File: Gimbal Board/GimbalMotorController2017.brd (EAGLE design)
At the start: 86.5 x 101.6 mm, 123 parts, among them J1 SL03THROUGH_HOLE, J3 APP_2POS_CONFIG5V_HORIZ, Q1 Q_IRF7437SMD, Q2 Q_IRF7437SMD, Q3 Q_IRF7437SMD, Q4 Q_IRF7437SMD, Q5 Q_IRF7437SMD, Q6 Q_IRF7437SMD, Q7 MOSFET-PCHANNEL, Q8 MOSFET-PCHANNEL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

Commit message: Fixed ERC issue
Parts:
- R14, R19, R24, R26: value 184k -> 191k
- R15, R20, R25, R27: value 50k -> 51.7k
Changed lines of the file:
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@@
 <attribute name="VALUE" x="71.34225" y="60.67425" size="0.4064" layer="27" font="vector" rot="R270"/>
 </element>
-<element name="R14" library="SparkFun-Passives" package="0805" value="184k" x="56.8325" y="39.0525" smashed="yes" rot="R180">
+<element name="R14" library="SparkFun-Passives" package="0805" value="191k" x="56.8325" y="39.0525" smashed="yes" rot="R180">
 <attribute name="NAME" x="54.737" y="39.8145" size="0.6096" layer="25" font="vector" rot="R270"/>
 <attribute name="VALUE" x="57.0865" y="40.1955" size="0.4064" layer="27" font="vector" rot="R180"/>
 </element>
-<element name="R15" library="SparkFun-Passives" package="0805" value="50k" x="56.8325" y="41.5925" smashed="yes">
+<element name="R15" library="SparkFun-Passives" package="0805" value="51.7k" x="56.8325" y="41.5925" smashed="yes">
 <attribute name="NAME" x="55.626" y="41.3385" size="0.6096" layer="25" font="vector" rot="R90"/>
 <attribute name="VALUE" x="55.8165" y="42.2275" size="0.4064" layer="27" font="vector"/>
@@
 <attribute name="VALUE" x="72.644" y="37.56025" size="0.4064" layer="27" font="vector" rot="R270"/>
 </element>
-<element name="R19" library="SparkFun-Passives" package="0805" value="184k" x="52.2605" y="39.0525" smashed="yes">
+<element name="R19" library="SparkFun-Passives" package="0805" value="191k" x="52.2605" y="39.0525" smashed="yes">
 <attribute name="NAME" x="50.8" y="38.5445" size="0.6096" layer="25" font="vector" rot="R90"/>
 <attribute name="VALUE" x="50.9905" y="39.9415" size="0.4064" layer="27" font="vector"/>
@@
 <attribute name="VALUE" x="38.1" y="42.2275" size="0.4064" layer="27" font="vector" rot="R270"/>
 </element>
-<element name="R20" library="SparkFun-Passives" package="0805" value="50k" x="52.2605" y="41.5925" smashed="yes" rot="R180">
+<element name="R20" library="SparkFun-Passives" package="0805" value="51.7k" x="52.2605" y="41.5925" smashed="yes" rot="R180">
 <attribute name="NAME" x="50.165" y="42.3545" size="0.6096" layer="25" font="vector" rot="R270"/>
 <attribute name="VALUE" x="52.5145" y="42.7355" size="0.4064" layer="27" font="vector" rot="R180"/>
@@
 <attribute name="VALUE" x="34.13125" y="68.961" size="0.4064" layer="27" font="vector" rot="R90"/>
 </element>
-<element name="R24" library="SparkFun-Passives" package="0805" value="184k" x="47.4345" y="39.0525" smashed="yes">
+<element name="R24" library="SparkFun-Passives" package="0805" value="191k" x="47.4345" y="39.0525" smashed="yes">
 <attribute name="NAME" x="45.974" y="38.5445" size="0.6096" layer="25" font="vector" rot="R90"/>
 <attribute name="VALUE" x="46.1645" y="39.9415" size="0.4064" layer="27" font="vector"/>
 </element>
-<element name="R25" library="SparkFun-Passives" package="0805" value="50k" x="47.4345" y="41.5925" smashed="yes" rot="R180">
+<element name="R25" library="SparkFun-Passives" package="0805" value="51.7k" x="47.4345" y="41.5925" smashed="yes" rot="R180">
 <attribute name="NAME" x="45.339" y="42.6085" size="0.6096" layer="25" font="vector" rot="R270"/>
 <attribute name="VALUE" x="47.6885" y="42.7355" size="0.4064" layer="27" font="vector" rot="R180"/>
 </element>
-<element name="R26" library="SparkFun-Passives" package="0805" value="184k" x="61.6585" y="39.0525" smashed="yes" rot="R180">
+<element name="R26" library="SparkFun-Passives" package="0805" value="191k" x="61.6585" y="39.0525" smashed="yes" rot="R180">
 <attribute name="NAME" x="59.563" y="39.8145" size="0.6096" layer="25" font="vector" rot="R270"/>
 <attribute name="VALUE" x="62.1665" y="40.1955" size="0.4064" layer="27" font="vector" rot="R180"/>
 </element>
-<element name="R27" library="SparkFun-Passives" package="0805" value="50k" x="61.6585" y="41.5925" smashed="yes">
+<element name="R27" library="SparkFun-Passives" package="0805" value="51.7k" x="61.6585" y="41.5925" smashed="yes">
 <attribute name="NAME" x="59.69" y="41.7195" size="0.6096" layer="25" font="vector" rot="R270"/>
 <attribute name="VALUE" x="60.6425" y="42.4815" size="0.4064" layer="27" font="vector"/>

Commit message: Updated resistor values for new divider, updated indicators section, changed PWM_IN_NO_FILTER to PWM_IN and removed previous PWM_IN label
Resistor values updated for 12v to 3.2v ratio. Simplified D6 indicator schematic to be just an LED, resistor, power, and ground. Changed old PWM_IN_NO_FILTER label to PWM_IN in external connections, and removed old PWM_IN label from PA2 pin in external connections.
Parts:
- removed D16: 15V, SparkFun-DiscreteSemi:SOD-323
- removed Q9: MOSFET-NCHANNELAO3404A, SparkFun-DiscreteSemi:SOT23-3
- removed R50: 3M, SparkFun-Passives:0805
- removed R51: 1M, SparkFun-Passives:0805
- Q1, Q2, Q3, Q4, Q5, Q6: value Q_IRF7437SMD -> R6020ENJSMD
- R14, R19, R24, R26: value 191k -> 187k
- R15, R20, R25, R27: value 51.7k -> 68.1k
- R32: value 330 -> 1.2k
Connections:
- removed net N$36: C15.1
- removed net N$38: D16.C, Q9.1, R50.2, R51.1
- removed net N$41: D16.A, D6.A, Q9.2
- removed net PWM_IN_NO_FILTER: J1.3, U$2.PF4
- net GND: no longer R51.2
- net PVDD: now also C15.1, D6.A; no longer R50.1
- net PWM_IN: now also J1.3, U$2.PF4; no longer U$2.PA2
- net VCC: no longer Q9.3
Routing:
- net PWM_IN_NO_FILTER: track 17.7 -> 0.00 mm
- net PWM_IN: track 0.00 -> 17.7 mm
- net N$41: track 10.5 -> 0.00 mm
- net VCC: track 212.8 -> 202.4 mm
- net N$38: track 5.40 -> 0.00 mm
- net PVDD: track 79.1 -> 82.2 mm, vias 8 -> 7

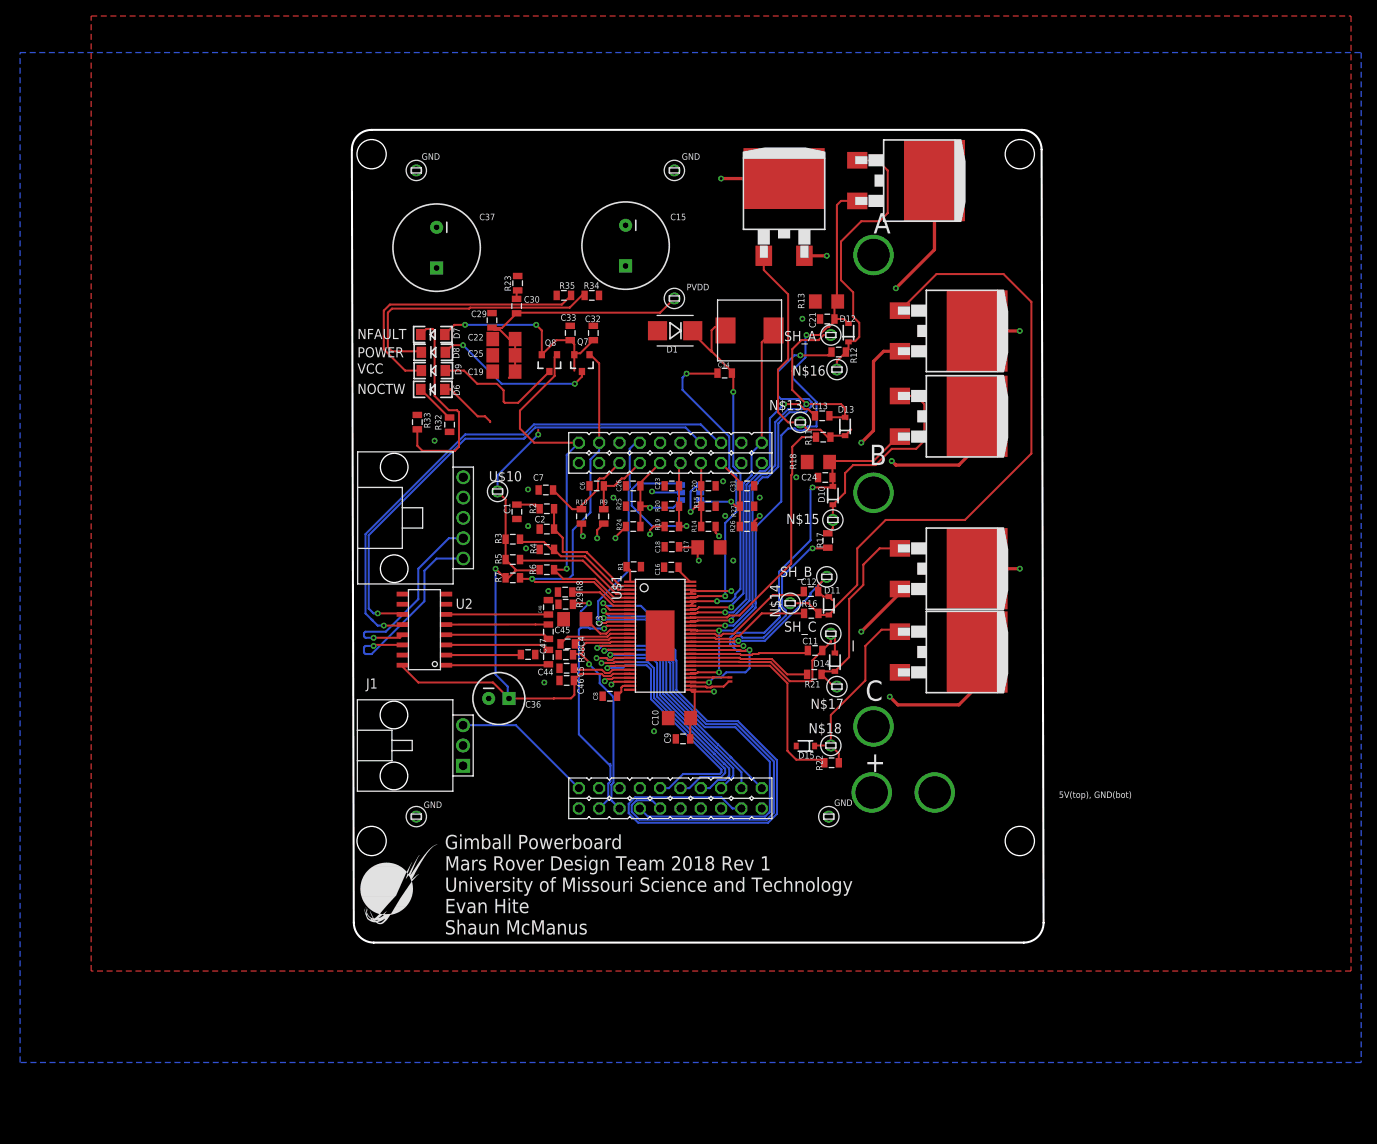
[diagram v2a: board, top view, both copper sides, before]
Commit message: Board routing was cleaned up. Silkscreen was cleaned up. Correct Package for Power Anderson Connectors is now being used.
Mounting holes were removed.  SL connectors were labelled. All test points are correctly named. More vias have been added to stitch the planes together. Traces were redrawn in many places for cleaner paths. Correct Vertical mounting board has been added. Anderson Power Package was changed to correct package. The inductor was moved to reduce noise. The power conditioning capacitor was moved out from under where the control card sits.
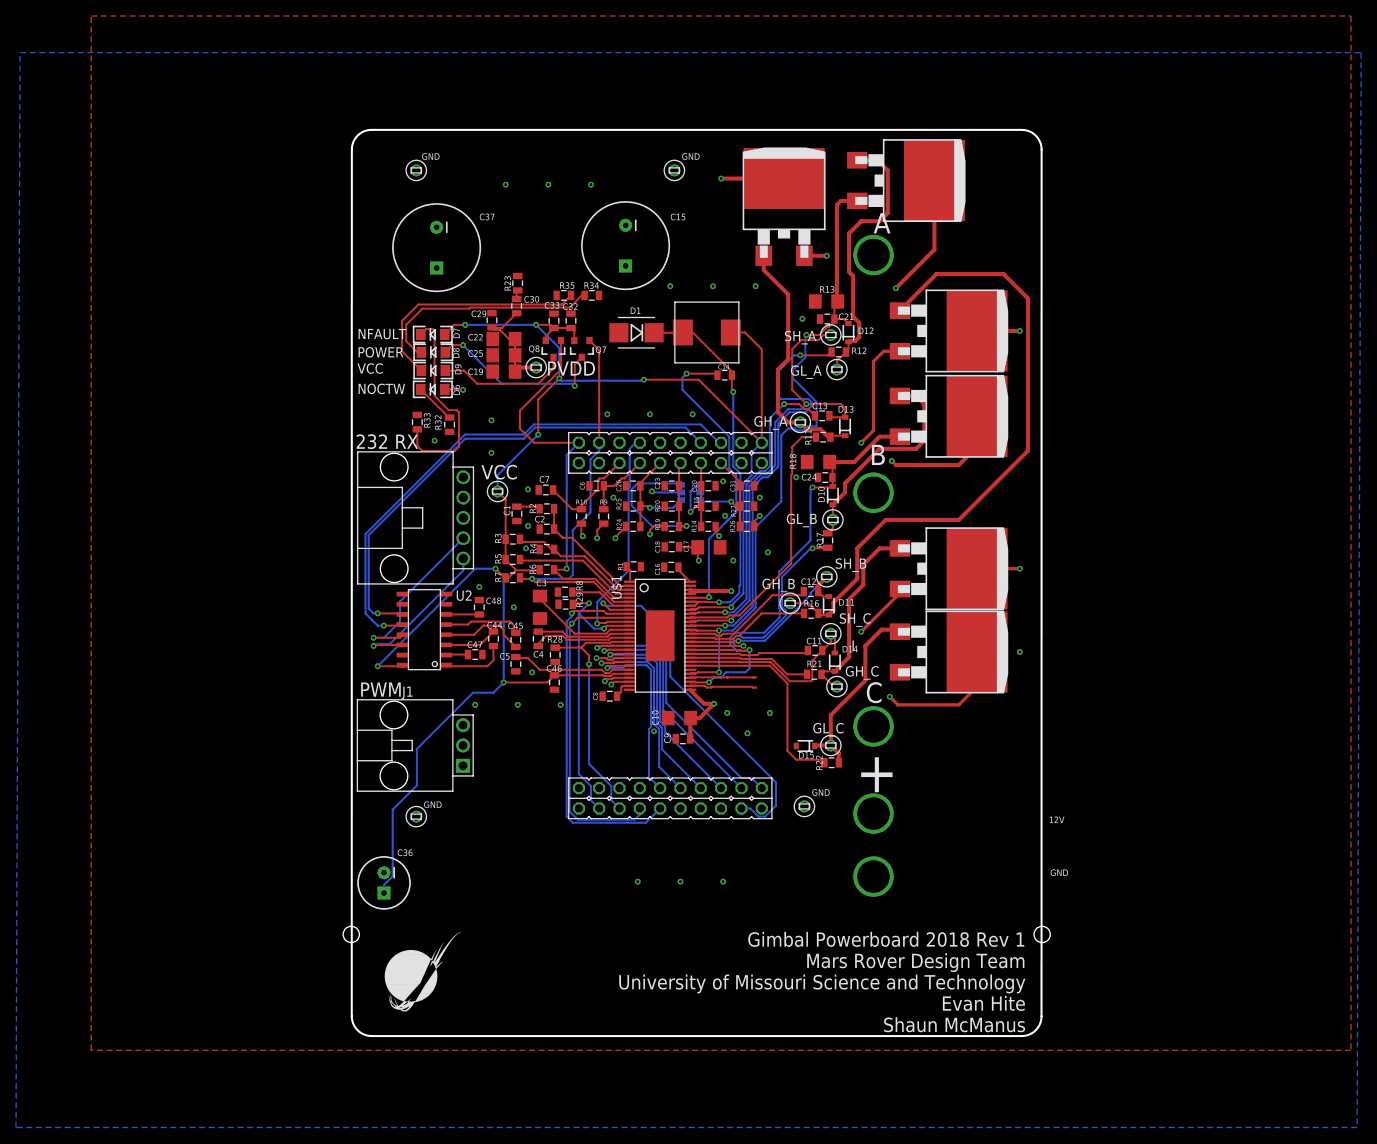
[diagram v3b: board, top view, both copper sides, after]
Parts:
- removed J3: APP_2POS_CONFIG5V_HORIZ, MRDT-Connectors:APP45_5V_HORIZ_CONFIG
- added J2: APP_2POS_CONFIG12V_HORIZ, MRDT-Connectors:APP45_12V_HORIZ_CONFIG
- moved C36 27.2 mm to (16.3, -5.49), turned to 270 degrees
- moved U$3 19.3 mm to (35.3, 58.9)
- moved U$9 11.3 mm to (16.4, -22.4)
- moved C48 8.64 mm to (28.2, 29.0)
- moved C44 7.23 mm to (30.0, 25.0)
- moved C47 6.60 mm to (27.7, 23.1)
- moved C5 6.37 mm to (32.8, 21.8), turned to 270 degrees
- moved U$14 5.34 mm to (56.6, 63.3)
- moved D1 4.83 mm to (47.8, 63.3)
- moved C3 4.60 mm to (35.8, 29.0), turned to 270 degrees
- moved C45 4.19 mm to (32.8, 24.9)
- moved C4 3.74 mm to (35.6, 25.0), turned to 270 degrees
- moved U$27 3.30 mm to (68.8, 4.06)
- moved C32 3.18 mm to (39.7, 64.8)
- moved SH1 3.14 mm to (62.6, 18.9)
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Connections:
- net GND: now also J2.GND; no longer J3.GND
- net PVDD: now also J2.12V; no longer J3.5V
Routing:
- net VCC: track 202.4 -> 244.6 mm, vias 6 -> 10
- net NSCS: track 79.5 -> 46.1 mm
- net PVDD: track 82.2 -> 58.8 mm, vias 7 -> 8
- net SDI: track 66.1 -> 46.0 mm
- net SDO: track 58.3 -> 41.4 mm
- net INL_C: track 33.8 -> 24.3 mm
- net N$45: track 12.8 -> 4.16 mm
- net N$9: track 7.71 -> 15.3 mm
- net N$8: track 6.46 -> 13.6 mm
- net INH_C: track 33.8 -> 26.9 mm
- net N$46: track 9.38 -> 2.78 mm
- net N$42: track 13.1 -> 6.62 mm
- net N$26: track 34.3 -> 28.5 mm
- net N$7: track 7.22 -> 12.5 mm
- net N$27: track 34.8 -> 29.7 mm
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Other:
- board size 86.5 x 101.6 mm -> 86.2 x 113.3 mm
- board text added: "232 RX"
- board text added: "GH_A"
- board text added: "GH_B"
- board text added: "GH_C"
- board text added: "GL_A"
- board text added: "GL_B"
- board text added: "GL_C"
- board text added: "Gimbal Powerboard 2018 Rev 1 Mars Rover Design Team University of Missouri Science and Technology Evan Hite Shaun McManus"
- board text added: "PWM"
- board text removed: "Gimball Powerboard Mars Rover Design Team 2018 Rev 1 University of Missouri Science and Technology Evan Hite Shaun McManus"
- board text removed: "N$13"
- board text removed: "N$14"
- board text removed: "N$15"
- board text removed: "N$16"
- board text removed: "N$17"
- board text removed: "N$18"
